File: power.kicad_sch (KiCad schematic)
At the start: 33 parts, among them U17 TPS62933, U6 TLV62569DBV, U8 INA190A2IDCKR, U9 TPS2121RUXR

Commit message: Route PMW3901B
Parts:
- removed D3: SMF14A, Diode_SMD:D_SMF, symbol Diode:SMF14A
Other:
- moved on the sheet: C65, C76, C77, C78, C79, C80, L5, R40, R41, R42, U17

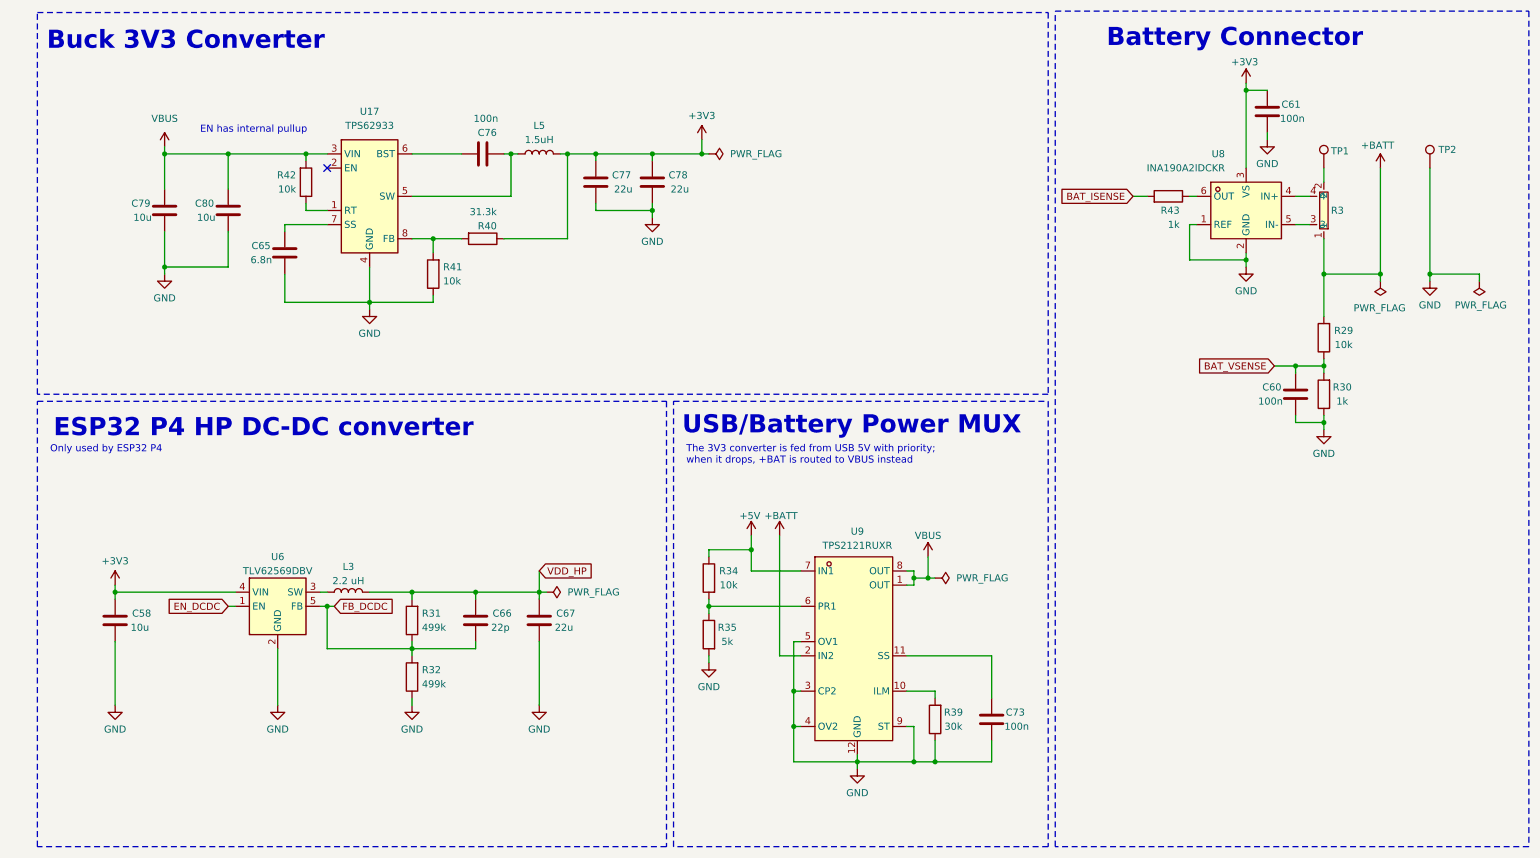
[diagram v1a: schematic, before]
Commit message: Fix BEMF comparator pinout
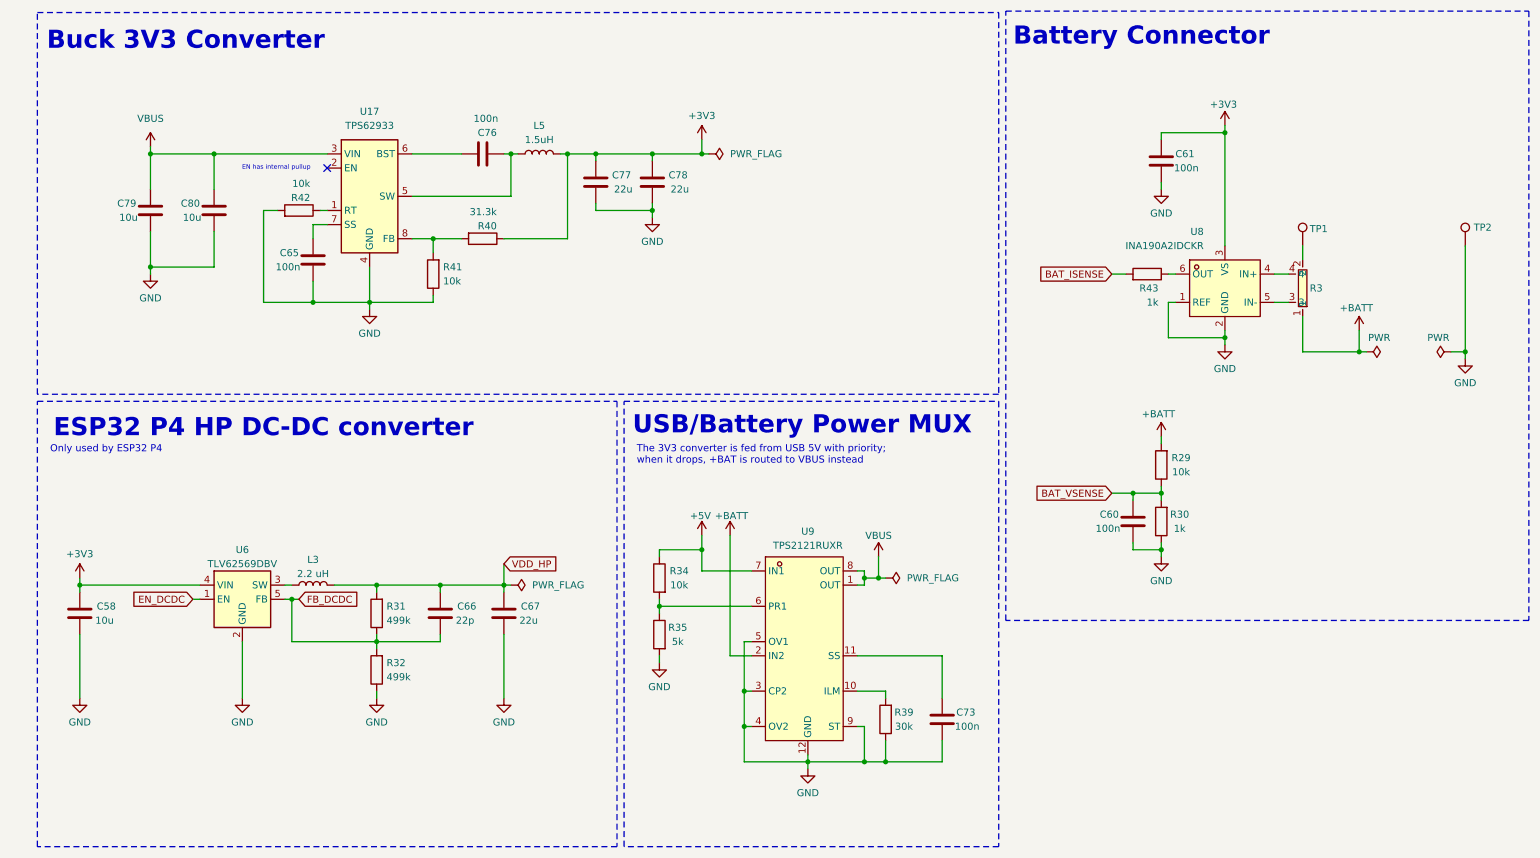
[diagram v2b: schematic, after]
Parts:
- C65: value 6.8n -> 100n
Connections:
- net GND: now also R42.2
- net VBUS: no longer R42.2
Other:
- company: All-in-one drone flight controller, camera and ESC -> All-in-one drone flight controller, camera and 2S-3S ESC
- moved on the sheet: C58, C60, C61, C65, C66, C67, C73, C79, C80, L3, R29, R3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

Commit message: Switch to 2.2 uH 1008 inductor for both DCDC converters
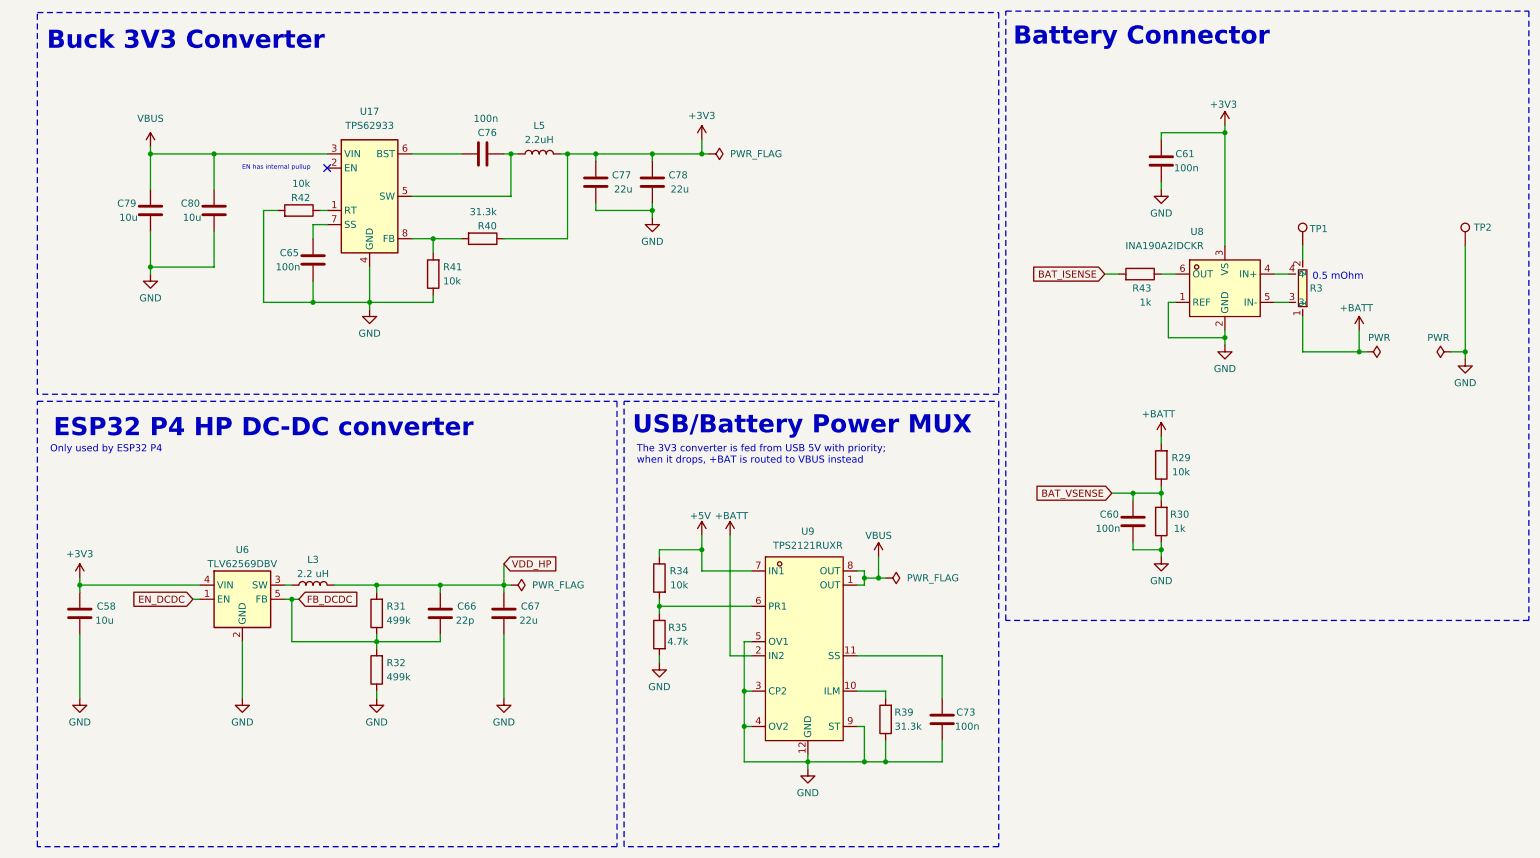
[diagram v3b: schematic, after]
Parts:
- C76: footprint Capacitor_SMD:C_0402_1005Metric -> Capacitor_SMD:C_0201_0603Metric
- L3: footprint easyeda2kicad:L0806 -> Inductor_SMD:L_1008_2520Metric
- L5: value 1.5uH -> 2.2uH
- R35: value 5k -> 4.7k
- R39: value 30k -> 31.3k
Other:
- note added: "0.5 mOhm"
- moved on the sheet: R43
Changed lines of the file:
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@@
 		)
 	)
+	(text "0.5 mOhm\n"
+		(exclude_from_sim no)
+		(at 247.65 61.468 0)
+		(effects
+			(font
+				(size 1.27 1.27)
+			)
+		)
+	)
 	(text "Battery Connector"
 		(exclude_from_sim no)
@@
 	(wire
 		(pts
-			(xy 207.01 60.96) (xy 209.55 60.96)
+			(xy 205.74 60.96) (xy 208.28 60.96)
 		)
 		(stroke
@@
 	(wire
 		(pts
-			(xy 217.17 60.96) (xy 218.44 60.96)
+			(xy 215.9 60.96) (xy 218.44 60.96)
 		)
 		(stroke
@@
 	(global_label "BAT_ISENSE"
 		(shape input)
-		(at 207.01 60.96 180)
+		(at 205.74 60.96 180)
 		(fields_autoplaced yes)
 		(effects
@@
 		)
 		(property "Intersheetrefs" "${INTERSHEET_REFS}"
-			(at 193.0787 60.96 0)
+			(at 191.8087 60.96 0)
 			(hide yes)
 			(show_name no)
@@
 	(symbol
 		(lib_id "Device:R")
-		(at 213.36 60.96 270)
+		(at 212.09 60.96 270)
 		(mirror x)
 		(unit 1)
@@
 		(dnp no)
 		(property "Reference" "R43"
-			(at 215.392 63.5 90)
+			(at 214.122 63.5 90)
 			(show_name no)
 			(do_not_autoplace no)
@@
 		)
 		(property "Value" "1k"
-			(at 215.392 66.04 90)
+			(at 214.122 66.04 90)
 			(show_name no)
 			(do_not_autoplace no)
@@
 		)
 		(property "Footprint" "Resistor_SMD:R_0201_0603Metric"
-			(at 213.36 62.738 90)
+			(at 212.09 62.738 90)
 			(hide yes)
 			(show_name no)
@@
 		)
 		(property "Datasheet" ""
-			(at 213.36 60.96 0)
+			(at 212.09 60.96 0)
 			(hide yes)
 			(show_name no)
@@
 		)
 		(property "Description" "Resistor"
-			(at 213.36 60.96 0)
+			(at 212.09 60.96 0)
 			(hide yes)
 			(show_name no)
@@
 			)
 		)
-		(property "Value" "5k"
+		(property "Value" "4.7k"
 			(at 129.032 127 0)
 			(show_name no)
@@
 			)
 		)
-		(property "Footprint" "Capacitor_SMD:C_0402_1005Metric"
+		(property "Footprint" "Capacitor_SMD:C_0201_0603Metric"
 			(at 97.79 38.4048 0)
 			(hide yes)
@@
 			)
 		)
-		(property "Value" "1.5uH"
+		(property "Value" "2.2uH"
 			(at 104.14 36.83 90)
 			(show_name no)
@@
 			)
 		)
-		(property "Footprint" "easyeda2kicad:L0806"
+		(property "Footprint" "Inductor_SMD:L_1008_2520Metric"
 			(at 63.5 116.84 0)
 			(hide yes)
@@
 			)
 		)
-		(property "Value" "30k"
-			(at 169.672 142.24 0)
+		(property "Value" "31.3k"
+			(at 170.434 142.24 0)
 			(show_name no)
 			(do_not_autoplace no)

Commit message: Consolidate BOM further
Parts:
- L3: value 2.2 uH -> 2.2uH
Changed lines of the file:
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@@
 			)
 		)
-		(property "Value" "2.2 uH"
+		(property "Value" "2.2uH"
 			(at 63.5 114.808 90)
 			(show_name no)

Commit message: Start filling out BOM with LCSC IDs
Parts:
- C66: LCSC Part (none) -> C161417
- C67: LCSC Part (none) -> C86295
- C77, C78: footprint Capacitor_SMD:C_0805_2012Metric -> Capacitor_SMD:C_0603_1608Metric; LCSC Part (none) -> C86295
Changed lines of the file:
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@@
 			)
 		)
+		(property "LCSC Part" "C161417"
+			(at 86.36 121.92 0)
+			(hide yes)
+			(show_name no)
+			(do_not_autoplace no)
+			(effects
+				(font
+					(size 1.27 1.27)
+				)
+			)
+		)
 		(pin "1"
 		)
@@
 			)
 		)
+		(property "LCSC Part" "C86295"
+			(at 97.79 121.92 0)
+			(hide yes)
+			(show_name no)
+			(do_not_autoplace no)
+			(effects
+				(font
+					(size 1.27 1.27)
+				)
+			)
+		)
 		(pin "1"
 		)
@@
 			)
 		)
-		(property "Footprint" "Capacitor_SMD:C_0805_2012Metric"
+		(property "Footprint" "Capacitor_SMD:C_0603_1608Metric"
 			(at 125.4252 40.64 0)
 			(hide yes)
@@
 			)
 		)
+		(property "LCSC Part" "C86295"
+			(at 124.46 44.45 0)
+			(hide yes)
+			(show_name no)
+			(do_not_autoplace no)
+			(effects
+				(font
+					(size 1.27 1.27)
+				)
+			)
+		)
 		(pin "1"
 		)
@@
 			)
 		)
-		(property "Footprint" "Capacitor_SMD:C_0805_2012Metric"
+		(property "Footprint" "Capacitor_SMD:C_0603_1608Metric"
 			(at 115.2652 40.64 0)
 			(hide yes)
@@
 			(at 114.3 44.45 0)
 			(hide yes)
+			(show_name no)
+			(do_not_autoplace no)
+			(effects
+				(font
+					(size 1.27 1.27)
+				)
+			)
+		)
+		(property "LCSC Part" "C86295"
+			(at 114.3 44.45 0)
+			(hide yes)

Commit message: Fill out most of BOM
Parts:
- L3, L5: LCSC Part (none) -> C42455362
- R29, R34, R41, R42: LCSC Part (none) -> C473048
- R30, R43: LCSC Part (none) -> C270365
- R31, R32: LCSC Part (none) -> C470889
- R35: LCSC Part (none) -> C270346
- R39, R40: LCSC Part (none) -> C473585
- U17: LCSC Part (none) -> C3200405
- U6: LCSC Part (none) -> C141836

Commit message: Finish BOM list
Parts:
- C58: LCSC Part (none) -> C182375
- C60, C61, C65, C73, C76: LCSC Part (none) -> C76939
- C79, C80: LCSC Part (none) -> C237493

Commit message: Rename project
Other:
- title: Anticopter Duo -> P4eregrine
